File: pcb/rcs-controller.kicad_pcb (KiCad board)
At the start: 2 copper layers, 45.6 x 73 mm, 108 parts, among them J1 00222-32051, J10 0022-232021, J2 0022-232021, J3 0022-232041, J4 Screw_Terminal_4_P3.50mm, J5 USB_C_Receptacle_USB2.0_14P, J6 Conn_01x03, J8 00222-32051, Q1 SI7465DP-T1-E3, Q2 SI7465DP-T1-E3, Q3 SI7465DP-T1-E3, Q4 PMV45EN2, Q5 PMV45EN2, SW1 SW_Push, SW2 SW_Push, U1 LSM6DSOX, U2 MP26123DR-LF-Z, U3 TPS63070, U4 ESP32-S3-WROOM-1

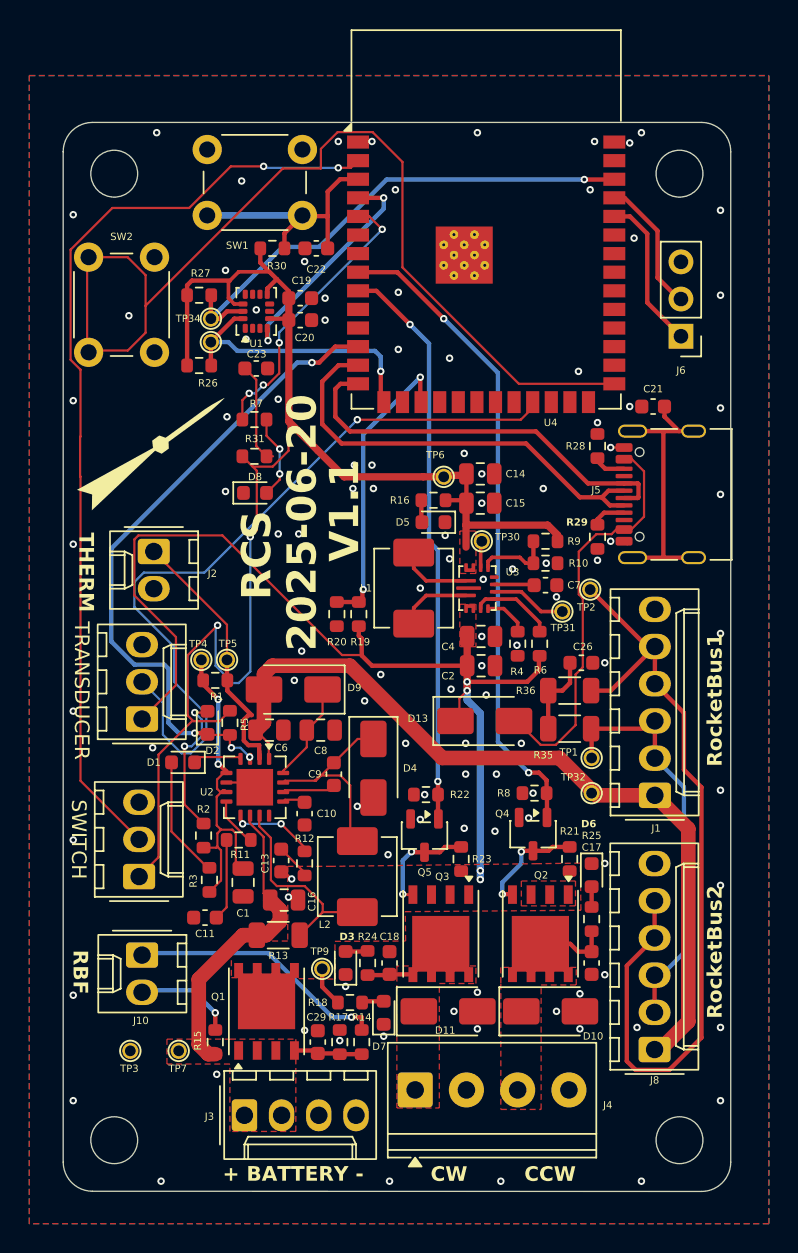
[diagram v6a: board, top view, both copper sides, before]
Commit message: Added voltage divider for transducer and fixed connector identifier issue
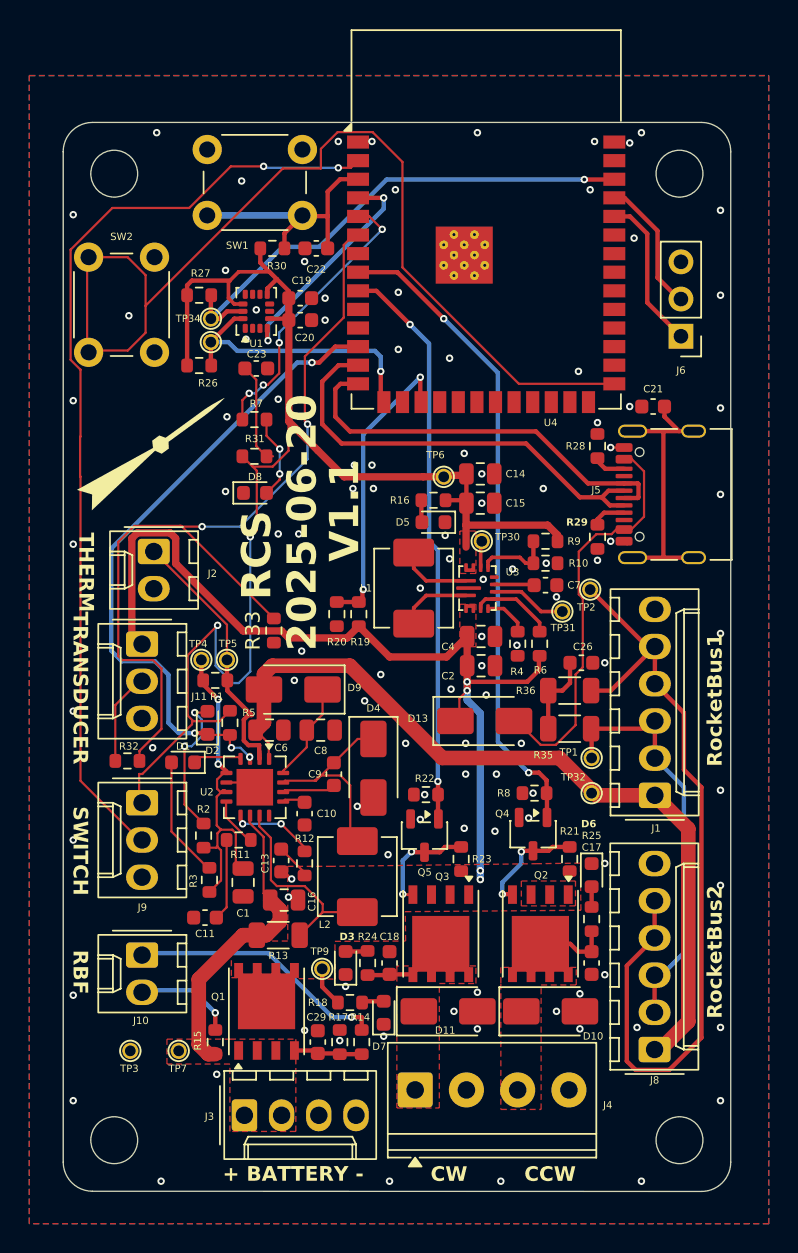
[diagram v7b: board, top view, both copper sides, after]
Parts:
- removed SWITCH, TRANSDUCER: Conn_01x03, Connector_Molex:Molex_KK-254_AE-6410-03A_1x03_P2.54mm_Vertical
- added J11: Conn_01x03, Connector_Molex:Molex_KK-254_AE-6410-03A_1x03_P2.54mm_Vertical, F.Cu at (105.5, 113.8)
- added J9: Conn_01x03, Connector_Molex:Molex_KK-254_AE-6410-03A_1x03_P2.54mm_Vertical, F.Cu at (105.5, 124.7)
- added R32: 10k, Resistor_SMD:R_0603_1608Metric, F.Cu at (104.5, 121.8)
- added R33: 15k, Resistor_SMD:R_0603_1608Metric, F.Cu at (114.5, 112.9)
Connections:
- U4 pad 23: Net-(J11-Pin_2) -> unconnected-(U4-IO21-Pad23)
- U4 pad 6: unconnected-(U4-IO6-Pad6) -> Net-(U4-IO6)
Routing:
- net Net-(U4-IO6): track 0.00 -> 59.4 mm, vias 0 -> 2
- net Net-(J11-Pin_2): track 53.3 -> 6.11 mm, vias 1 -> 0
- net VBUS: track 72.2 -> 65.9 mm
- net +3.3V: track 110.0 -> 105.0 mm
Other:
- board text added: "SWITCH"
- board text added: "TRANSDUCER"
